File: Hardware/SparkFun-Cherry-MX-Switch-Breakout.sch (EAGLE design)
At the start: 20 parts

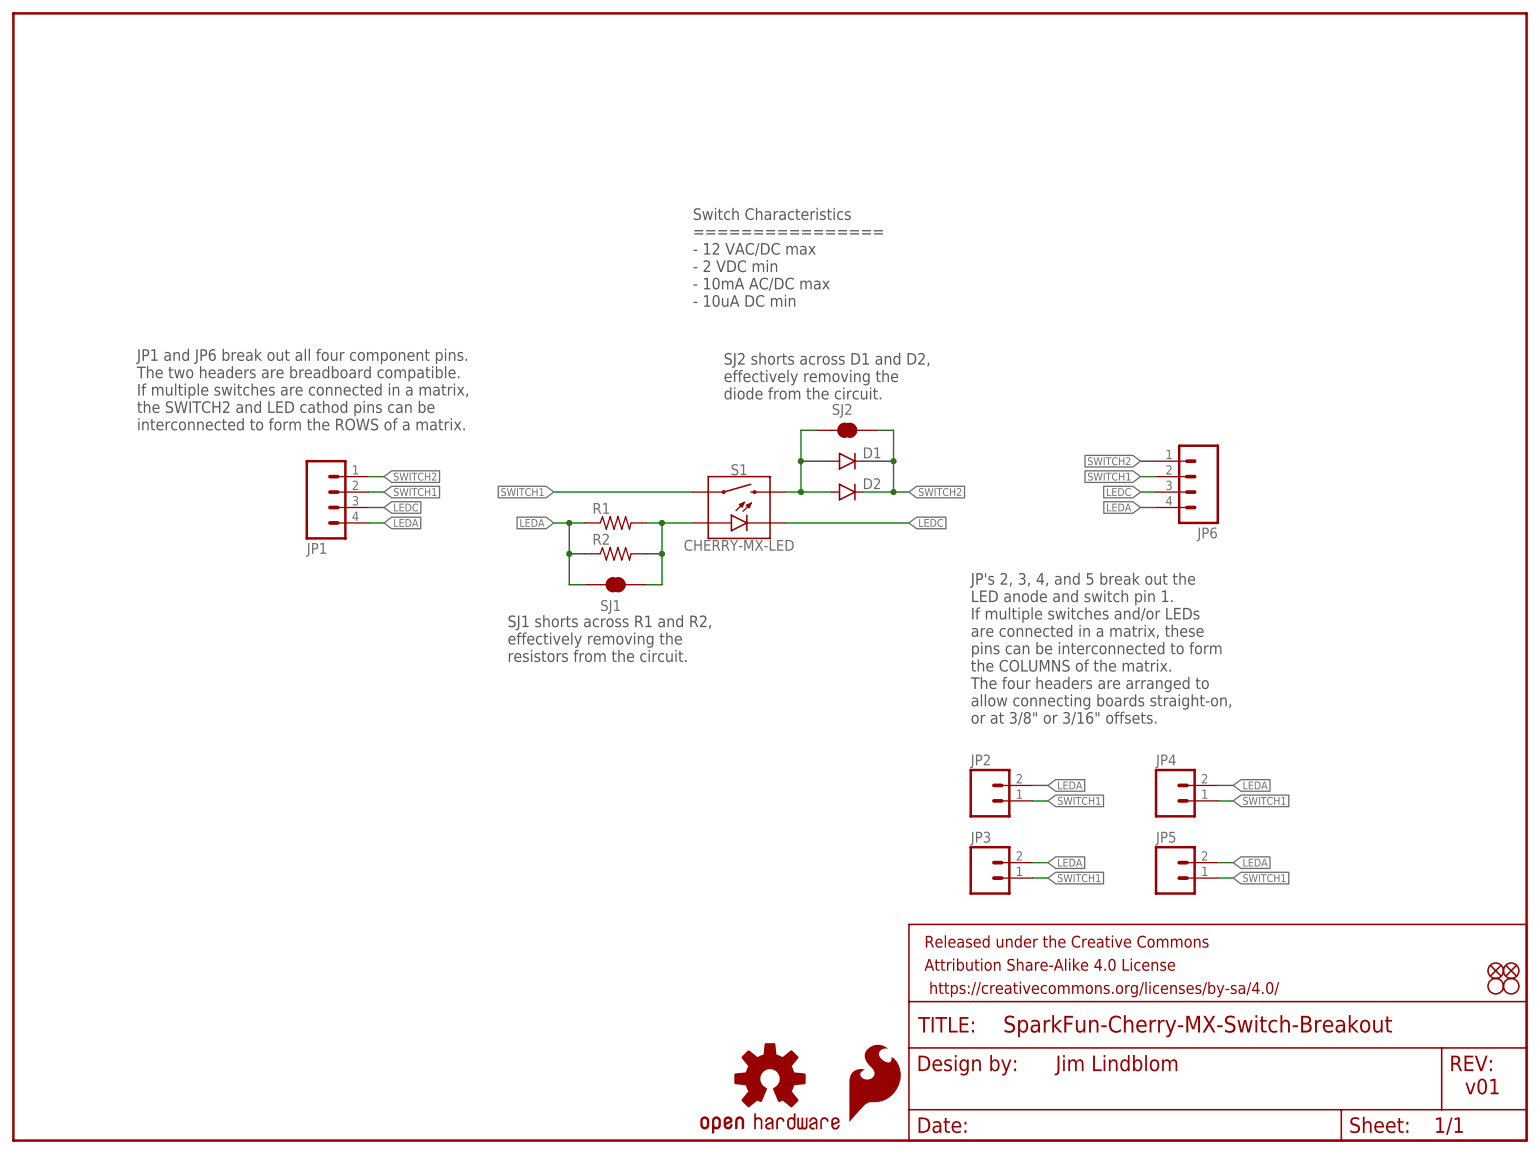
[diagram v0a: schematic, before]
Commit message: Rearranging resistor and diode packages and standoffs.
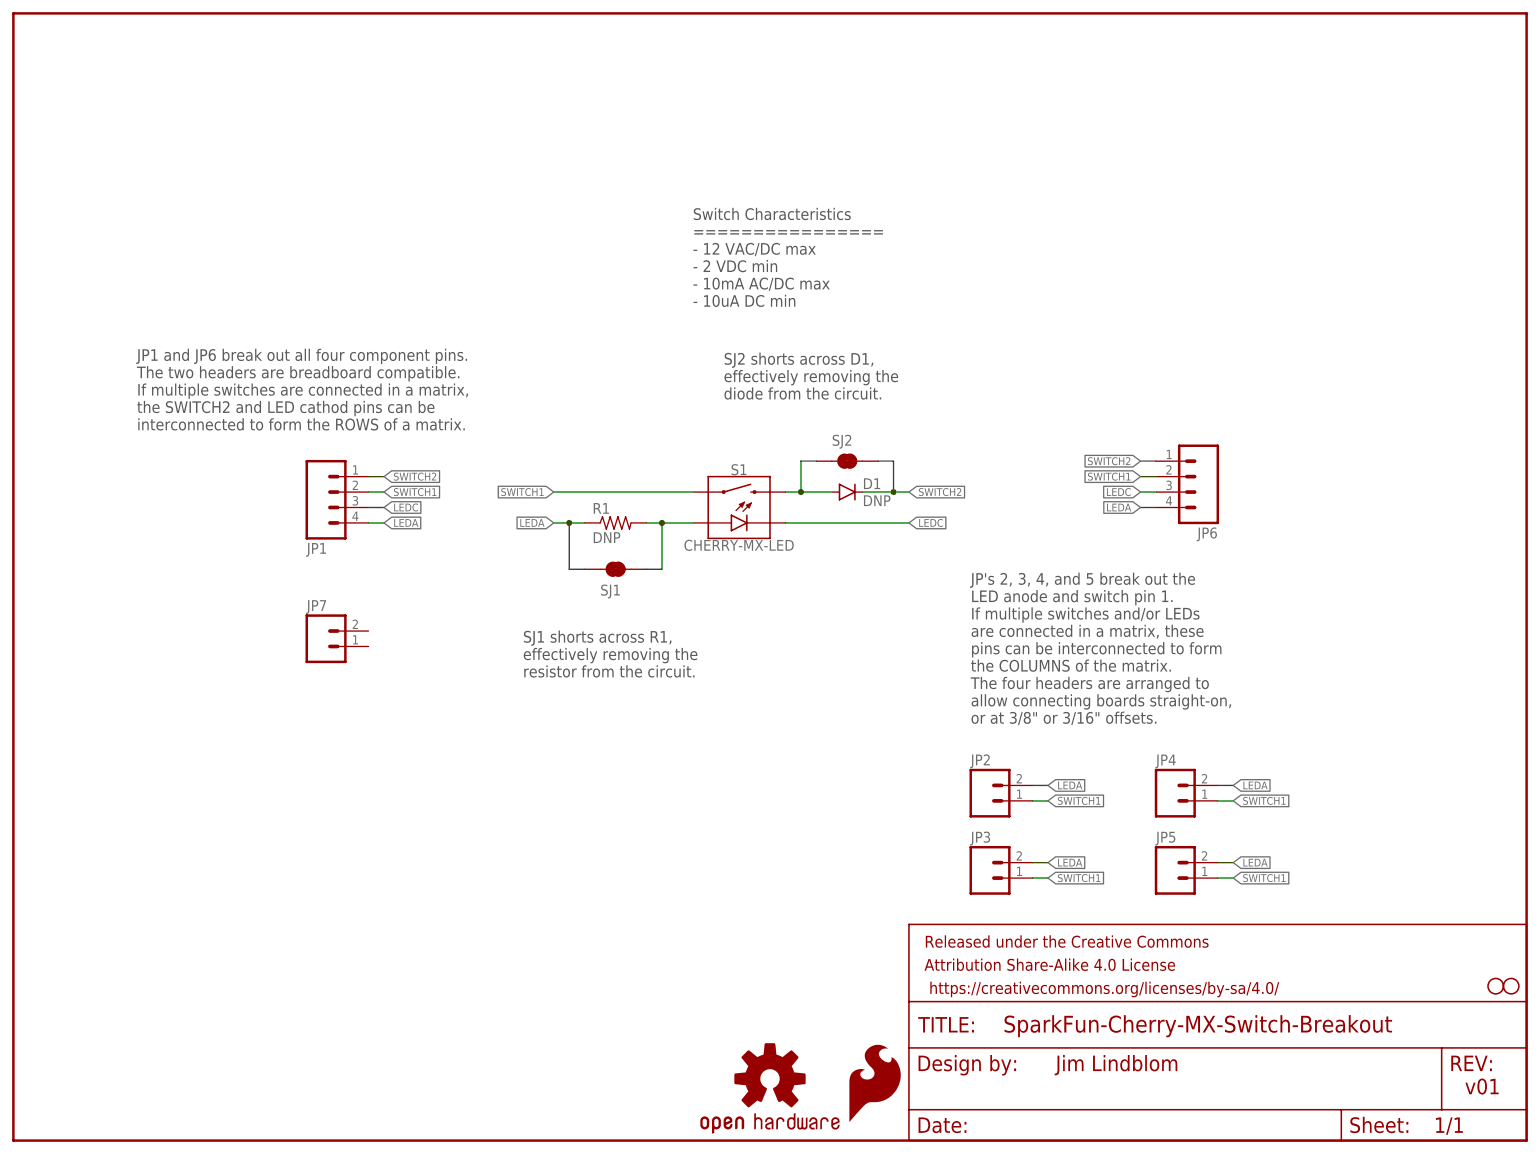
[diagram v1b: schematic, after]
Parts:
- removed D2: (no value), cherry-temp:DIODE1N4148-TIGHT
- removed FID1, FID2: FIDUCIAL1X2, SparkFun-Aesthetics:FIDUCIAL1X2
- removed R2: (no value), SparkFun-Resistors:RESISTOR0603
- added JP7: (no value), SparkFun-Connectors:M021X02_NO_SILK
- D1: value (none) -> DNP; device SparkFun-DiscreteSemi:DIODEBAS16 -> cherry-temp:DIODEPTH-VERT-0.1
- R1: value (none) -> DNP; device SparkFun-Resistors:RESISTORPTH-1/6W -> SparkFun-Resistors:RESISTORPTH-1/4W-VERT
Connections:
- net LEDA: no longer R2.1
- net N$1: no longer R2.2
- net N$3: no longer D2.A
- net SWITCH2: no longer D2.C
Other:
- note added: "SJ1 shorts across R1, effectively removing the resistor from the circuit."
- note added: "SJ2 shorts across D1, effectively removing the diode from the circuit."
- note removed: "SJ1 shorts across R1 and R2, effectively removing the resistors from the circuit."
- note removed: "SJ2 shorts across D1 and D2, effectively removing the diode from the circuit."
- moved on the sheet: D1, SJ1, SJ2
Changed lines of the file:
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@@
 <part name="FRAME1" library="SparkFun-Aesthetics" deviceset="FRAME-LETTER" device=""/>
 <part name="S1" library="cherry-temp" deviceset="CHERRY-MX-LED" device=""/>
-<part name="R1" library="SparkFun-Resistors" deviceset="RESISTOR" device="PTH-1/6W"/>
-<part name="D2" library="cherry-temp" deviceset="DIODE" device="1N4148-TIGHT"/>
+<part name="R1" library="SparkFun-Resistors" deviceset="RESISTOR" device="PTH-1/4W-VERT" value="DNP"/>
+<part name="D1" library="cherry-temp" deviceset="DIODE" device="PTH-VERT-0.1" value="DNP"/>
 <part name="SJ1" library="SparkFun-Passives" deviceset="JUMPER-PAD-2-NC_BY_TRACE" device="NO_SILK" value=""/>
 <part name="SJ2" library="SparkFun-Passives" deviceset="JUMPER-PAD-2-NC_BY_TRACE" device="NO_SILK" value=""/>
@@
 <part name="STANDOFF2" library="cherry-temp" deviceset="STAND-OFF" device="2-56"/>
 <part name="STANDOFF1" library="cherry-temp" deviceset="STAND-OFF" device="2-56"/>
-<part name="R2" library="SparkFun-Resistors" deviceset="RESISTOR" device="0603"/>
-<part name="D1" library="SparkFun-DiscreteSemi" deviceset="DIODE" device="BAS16"/>
-<part name="FID1" library="SparkFun-Aesthetics" deviceset="FIDUCIAL" device="1X2"/>
-<part name="FID2" library="SparkFun-Aesthetics" deviceset="FIDUCIAL" device="1X2"/>
+<part name="JP7" library="SparkFun-Connectors" deviceset="M02" device="1X02_NO_SILK"/>
 </parts>
 <sheets>
@@
 <text x="238.76" y="7.62" size="2.54" layer="94">v01</text>
 <text x="171.45" y="11.43" size="2.54" layer="94">Jim Lindblom</text>
-<text x="81.28" y="86.36" size="1.905" layer="97" align="top-left">SJ1 shorts across R1 and R2,
+<text x="83.82" y="83.82" size="1.905" layer="97" align="top-left">SJ1 shorts across R1,
 effectively removing the
-resistors from the circuit.</text>
-<text x="116.84" y="121.92" size="1.905" layer="97">SJ2 shorts across D1 and D2,
+resistor from the circuit.</text>
+<text x="116.84" y="121.92" size="1.905" layer="97">SJ2 shorts across D1,
 effectively removing the
 diode from the circuit.</text>
@@
 <instance part="S1" gate="G$1" x="119.38" y="104.14"/>
 <instance part="R1" gate="G$1" x="99.06" y="101.6"/>
-<instance part="D2" gate="G$1" x="137.16" y="106.68"/>
-<instance part="SJ1" gate="G$1" x="99.06" y="91.44" rot="MR180"/>
-<instance part="SJ2" gate="G$1" x="137.16" y="116.84"/>
+<instance part="D1" gate="G$1" x="137.16" y="106.68"/>
+<instance part="SJ1" gate="G$1" x="99.06" y="93.98" rot="MR180"/>
+<instance part="SJ2" gate="G$1" x="137.16" y="111.76"/>
 <instance part="JP1" gate="G$1" x="53.34" y="106.68" rot="MR180"/>
 <instance part="JP6" gate="G$1" x="193.04" y="109.22" rot="R180"/>
@@
 <instance part="STANDOFF2" gate="G$1" x="246.38" y="25.4"/>
 <instance part="STANDOFF1" gate="G$1" x="243.84" y="25.4"/>
-<instance part="R2" gate="G$1" x="99.06" y="96.52"/>
-<instance part="D1" gate="G$1" x="137.16" y="111.76"/>
-<instance part="FID1" gate="G$1" x="246.38" y="27.94"/>
-<instance part="FID2" gate="G$1" x="243.84" y="27.94"/>
+<instance part="JP7" gate="G$1" x="50.8" y="81.28"/>
 </instances>
 <busses>
@@
 <pinref part="SJ1" gate="G$1" pin="2"/>
 <wire x1="106.68" y1="101.6" x2="104.14" y2="101.6" width="0.1524" layer="91"/>
-<wire x1="104.14" y1="91.44" x2="106.68" y2="91.44" width="0.1524" layer="91"/>
-<wire x1="106.68" y1="91.44" x2="106.68" y2="96.52" width="0.1524" layer="91"/>
+<wire x1="104.14" y1="93.98" x2="106.68" y2="93.98" width="0.1524" layer="91"/>
 <junction x="106.68" y="101.6"/>
-<pinref part="R2" gate="G$1" pin="2"/>
-<wire x1="106.68" y1="96.52" x2="106.68" y2="101.6" width="0.1524" layer="91"/>
-<wire x1="104.14" y1="96.52" x2="106.68" y2="96.52" width="0.1524" layer="91"/>
-<junction x="106.68" y="96.52"/>
+<wire x1="106.68" y1="93.98" x2="106.68" y2="101.6" width="0.1524" layer="91"/>
 </segment>
 </net>
@@
 <segment>
 <pinref part="SJ1" gate="G$1" pin="1"/>
-<wire x1="93.98" y1="91.44" x2="91.44" y2="91.44" width="0.1524" layer="91"/>
-<wire x1="91.44" y1="91.44" x2="91.44" y2="96.52" width="0.1524" layer="91"/>
+<wire x1="93.98" y1="93.98" x2="91.44" y2="93.98" width="0.1524" layer="91"/>
 <pinref part="R1" gate="G$1" pin="1"/>
-<wire x1="91.44" y1="96.52" x2="91.44" y2="101.6" width="0.1524" layer="91"/>
+<wire x1="91.44" y1="93.98" x2="91.44" y2="101.6" width="0.1524" layer="91"/>
 <wire x1="91.44" y1="101.6" x2="93.98" y2="101.6" width="0.1524" layer="91"/>
 <wire x1="91.44" y1="101.6" x2="88.9" y2="101.6" width="0.1524" layer="91"/>
 <junction x="91.44" y="101.6"/>
 <label x="88.9" y="101.6" size="1.27" layer="95" rot="R180" xref="yes"/>
-<pinref part="R2" gate="G$1" pin="1"/>
-<wire x1="93.98" y1="96.52" x2="91.44" y2="96.52" width="0.1524" layer="91"/>
-<junction x="91.44" y="96.52"/>
 </segment>
 <segment>
@@
 <segment>
 <pinref part="S1" gate="G$1" pin="S2"/>
-<pinref part="D2" gate="G$1" pin="A"/>
+<pinref part="D1" gate="G$1" pin="A"/>
 <wire x1="127" y1="106.68" x2="129.54" y2="106.68" width="0.1524" layer="91"/>
 <wire x1="129.54" y1="106.68" x2="134.62" y2="106.68" width="0.1524" layer="91"/>
-<wire x1="129.54" y1="106.68" x2="129.54" y2="111.76" width="0.1524" layer="91"/>
 <junction x="129.54" y="106.68"/>
 <pinref part="SJ2" gate="G$1" pin="1"/>
-<wire x1="129.54" y1="111.76" x2="129.54" y2="116.84" width="0.1524" layer="91"/>
-<wire x1="129.54" y1="116.84" x2="132.08" y2="116.84" width="0.1524" layer="91"/>
-<pinref part="D1" gate="G$1" pin="A"/>
-<wire x1="134.62" y1="111.76" x2="129.54" y2="111.76" width="0.1524" layer="91"/>
-<junction x="129.54" y="111.76"/>
+<wire x1="129.54" y1="106.68" x2="129.54" y2="111.76" width="0.1524" layer="91"/>
+<wire x1="129.54" y1="111.76" x2="132.08" y2="111.76" width="0.1524" layer="91"/>
 </segment>
 </net>
@@
 <segment>
 <pinref part="SJ2" gate="G$1" pin="2"/>
-<wire x1="142.24" y1="116.84" x2="144.78" y2="116.84" width="0.1524" layer="91"/>
-<wire x1="144.78" y1="116.84" x2="144.78" y2="111.76" width="0.1524" layer="91"/>
-<pinref part="D2" gate="G$1" pin="C"/>
+<wire x1="142.24" y1="111.76" x2="144.78" y2="111.76" width="0.1524" layer="91"/>
+<pinref part="D1" gate="G$1" pin="C"/>
 <wire x1="144.78" y1="111.76" x2="144.78" y2="106.68" width="0.1524" layer="91"/>
 <wire x1="144.78" y1="106.68" x2="139.7" y2="106.68" width="0.1524" layer="91"/>
@@
 <junction x="144.78" y="106.68"/>
 <label x="147.32" y="106.68" size="1.27" layer="95" xref="yes"/>
-<pinref part="D1" gate="G$1" pin="C"/>
-<wire x1="139.7" y1="111.76" x2="144.78" y2="111.76" width="0.1524" layer="91"/>
-<junction x="144.78" y="111.76"/>
 </segment>
 <segment>
